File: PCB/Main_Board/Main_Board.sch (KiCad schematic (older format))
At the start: 12 parts, among them J1 USB_B_Micro, J2 Screw_Terminal_01x02, J3 SJ1-3523N, J4 SJ1-3523N, J5 Screw_Terminal_01x04, J6 Screw_Terminal_01x06, SW1 SW_SPDT, U1 TLV75533PDBV

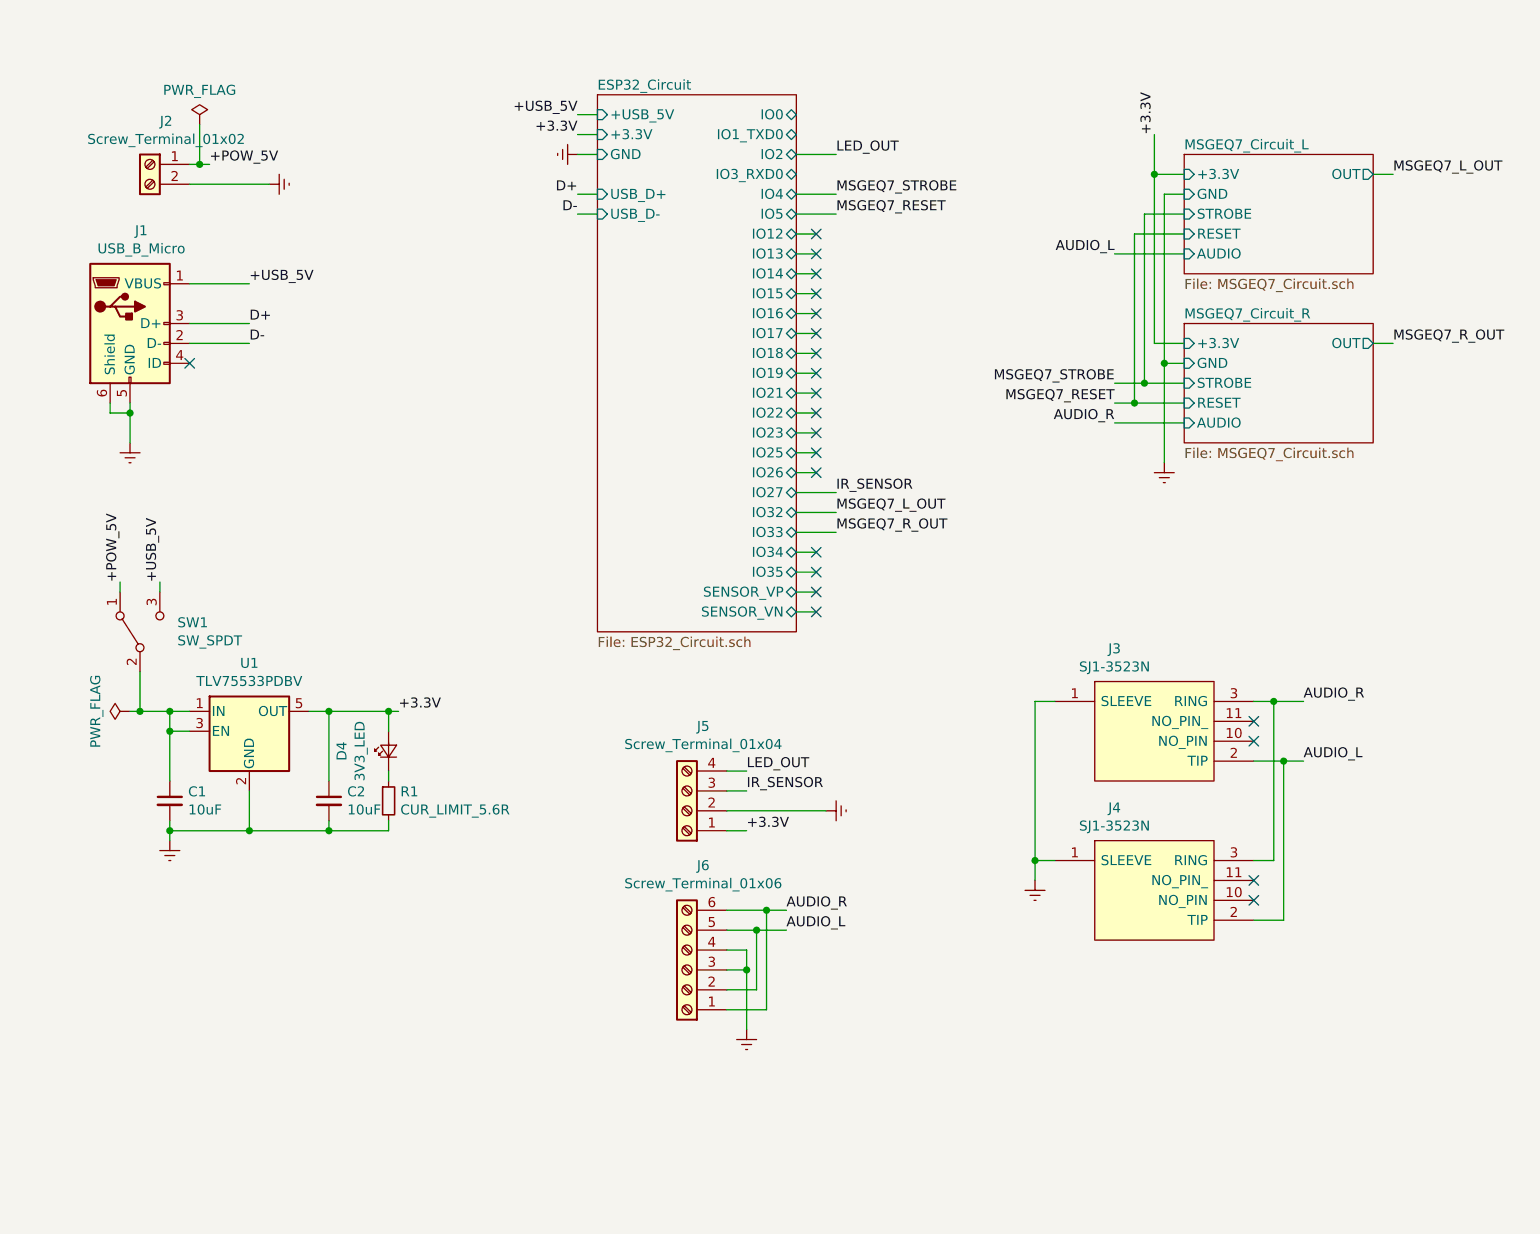
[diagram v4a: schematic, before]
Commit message: Add level shifter and further PCB work
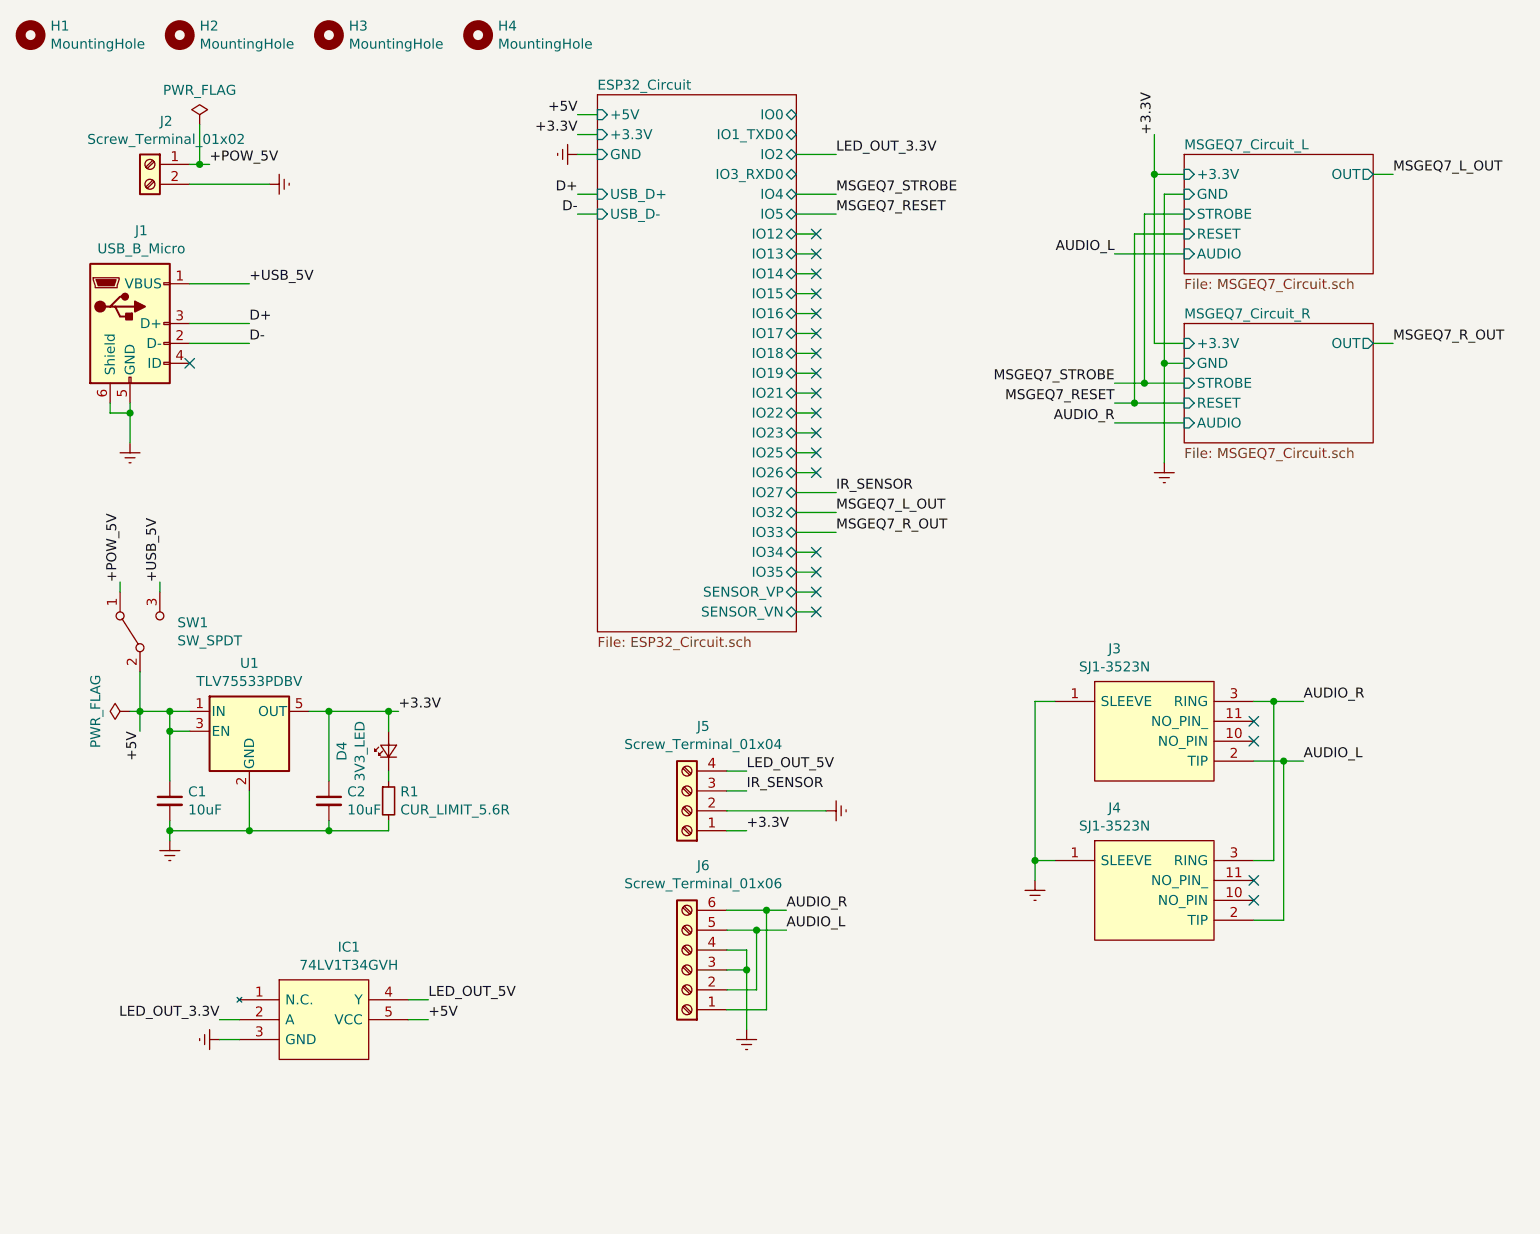
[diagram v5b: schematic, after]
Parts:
- added H1, H2, H3, H4: MountingHole, MountingHole:MountingHole_3.2mm_M3, symbol Mechanical:MountingHole
- added IC1: 74LV1T34GVH, SamacSys:SOT95P275X110-5N, symbol SamacSys:74LV1T34GVH
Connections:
- net Earth: now also IC1.3 (GND)
- net +5V: now reaches C1.1, SW1.2 (B), U1.1 (IN), U1.3 (EN)
- net +5V: now also IC1.5 (VCC)
- net LED_OUT renamed LED_OUT_5V
- net LED_OUT_5V: now also IC1.4 (Y)
- new net LED_OUT_3.3V: IC1.2 (A)
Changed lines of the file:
@@
 F1 "ESP32_Circuit.sch" 50
 F2 "+3.3V" I L 3500 1150 50
-F3 "+USB_5V" I L 3500 1050 50
-F4 "GND" I L 3500 1250 50
-F5 "USB_D-" I L 3500 1550 50
-F6 "USB_D+" I L 3500 1450 50
-F7 "IO35" B R 4500 3350 50
-F8 "IO33" B R 4500 3150 50
-F9 "IO34" B R 4500 3250 50
-F10 "IO32" B R 4500 3050 50
-F11 "IO27" B R 4500 2950 50
-F12 "IO26" B R 4500 2850 50
-F13 "IO25" B R 4500 2750 50
-F14 "IO23" B R 4500 2650 50
-F15 "IO22" B R 4500 2550 50
-F16 "IO21" B R 4500 2450 50
-F17 "IO19" B R 4500 2350 50
-F18 "IO18" B R 4500 2250 50
-F19 "IO17" B R 4500 2150 50
-F20 "IO16" B R 4500 2050 50
-F21 "IO15" B R 4500 1950 50
-F22 "IO14" B R 4500 1850 50
-F23 "IO13" B R 4500 1750 50
-F24 "IO12" B R 4500 1650 50
-F25 "IO5" B R 4500 1550 50
-F26 "IO4" B R 4500 1450 50
-F27 "IO2" B R 4500 1250 50
-F28 "IO3_RXD0" B R 4500 1350 50
-F29 "IO1_TXD0" B R 4500 1150 50
-F30 "IO0" B R 4500 1050 50
-F31 "SENSOR_VP" B R 4500 3450 50
-F32 "SENSOR_VN" B R 4500 3550 50
+F3 "GND" I L 3500 1250 50
+F4 "USB_D-" I L 3500 1550 50
+F5 "USB_D+" I L 3500 1450 50
+F6 "IO35" B R 4500 3350 50
+F7 "IO33" B R 4500 3150 50
+F8 "IO34" B R 4500 3250 50
+F9 "IO32" B R 4500 3050 50
+F10 "IO27" B R 4500 2950 50
+F11 "IO26" B R 4500 2850 50
+F12 "IO25" B R 4500 2750 50
+F13 "IO23" B R 4500 2650 50
+F14 "IO22" B R 4500 2550 50
+F15 "IO21" B R 4500 2450 50
+F16 "IO19" B R 4500 2350 50
+F17 "IO18" B R 4500 2250 50
+F18 "IO17" B R 4500 2150 50
+F19 "IO16" B R 4500 2050 50
+F20 "IO15" B R 4500 1950 50
+F21 "IO14" B R 4500 1850 50
+F22 "IO13" B R 4500 1750 50
+F23 "IO12" B R 4500 1650 50
+F24 "IO5" B R 4500 1550 50
+F25 "IO4" B R 4500 1450 50
+F26 "IO2" B R 4500 1250 50
+F27 "IO3_RXD0" B R 4500 1350 50
+F28 "IO1_TXD0" B R 4500 1150 50
+F29 "IO0" B R 4500 1050 50
+F30 "SENSOR_VP" B R 4500 3450 50
+F31 "SENSOR_VN" B R 4500 3550 50
+F32 "+5V" I L 3500 1050 50
 $EndSheet
 Text Label 3400 1050 2    50   ~ 0
-+USB_5V
++5V
 Text Label 3400 1150 2    50   ~ 0
 +3.3V
@@
 MSGEQ7_STROBE
 Text Label 4250 4350 0    50   ~ 0
-LED_OUT
+LED_OUT_5V
 Text Label 4700 3050 0    50   ~ 0
 MSGEQ7_L_OUT
@@
 	4500 3150 4700 3150
 Text Label 4700 1250 0    50   ~ 0
-LED_OUT
+LED_OUT_3.3V
 Wire Wire Line
 	4500 1250 4700 1250
@@
 Wire Wire Line
 	4150 4550 4650 4550
+Text Label 1200 4150 3    50   ~ 0
++5V
+Wire Wire Line
+	1200 4150 1200 4050
+$Comp
+L SamacSys:74LV1T34GVH IC1
+U 1 1 5F6C379F
+P 1700 5500
+F 0 "IC1" H 2250 5765 50  0000 C CNN
+F 1 "74LV1T34GVH" H 2250 5674 50  0000 C CNN
+F 2 "SamacSys:SOT95P275X110-5N" H 2650 5600 50  0001 L CNN
+F 3 "https://assets.nexperia.com/documents/data-sheet/74LV1T34.pdf" H 2650 5500 50  0001 L CNN
+F 4 "Buffers & Line Drivers BUFFER LINE DRIVER" H 2650 5400 50  0001 L CNN "Description"
+F 5 "1.1" H 2650 5300 50  0001 L CNN "Height"
+F 6 "771-74LV1T34GVH" H 2650 5200 50  0001 L CNN "Mouser Part Number"
+F 7 "https://www.mouser.co.uk/ProductDetail/Nexperia/74LV1T34GVH?qs=Cb2nCFKsA8oBEV51cGATww%3D%3D" H 2650 5100 50  0001 L CNN "Mouser Price/Stock"
+F 8 "Nexperia" H 2650 5000 50  0001 L CNN "Manufacturer_Name"
+F 9 "74LV1T34GVH" H 2650 4900 50  0001 L CNN "Manufacturer_Part_Number"
+	1    1700 5500
+	1    0    0    -1
+$EndComp
+Text Label 2650 5600 0    50   ~ 0
++5V
+Wire Wire Line
+	2650 5600 2550 5600
+$Comp
+L power:Earth #PWR0102
+U 1 1 5F6E2BBD
+P 1600 5700
+AR Path="/5F6E2BBD" Ref="#PWR0102"  Part="1"
+AR Path="/5F591C5D/5F6E2BBD" Ref="#PWR?"  Part="1"
+F 0 "#PWR0102" H 1600 5450 50  0001 C CNN
+F 1 "Earth" H 1600 5550 50  0001 C CNN
+F 2 "" H 1600 5700 50  0001 C CNN
+F 3 "~" H 1600 5700 50  0001 C CNN
+	1    1600 5700
+	0    1    1    0
+$EndComp
+Wire Wire Line
+	1600 5700 1700 5700
+Text Label 1600 5600 2    50   ~ 0
+LED_OUT_3.3V
+Wire Wire Line
+	1600 5600 1700 5600
+Text Label 2650 5500 0    50   ~ 0
+LED_OUT_5V
+Wire Wire Line
+	2650 5500 2550 5500
+$Comp
+L Mechanical:MountingHole H1
+U 1 1 5F70586C
+P 650 650
+F 0 "H1" H 750 696 50  0000 L CNN
+F 1 "MountingHole" H 750 605 50  0000 L CNN
+F 2 "MountingHole:MountingHole_3.2mm_M3" H 650 650 50  0001 C CNN
+F 3 "~" H 650 650 50  0001 C CNN
+	1    650  650
+	1    0    0    -1
+$EndComp
+$Comp
+L Mechanical:MountingHole H2
+U 1 1 5F706754
+P 1400 650
+F 0 "H2" H 1500 696 50  0000 L CNN
+F 1 "MountingHole" H 1500 605 50  0000 L CNN
+F 2 "MountingHole:MountingHole_3.2mm_M3" H 1400 650 50  0001 C CNN
+F 3 "~" H 1400 650 50  0001 C CNN
+	1    1400 650
+	1    0    0    -1
+$EndComp
+$Comp
+L Mechanical:MountingHole H3
+U 1 1 5F70733F
+P 2150 650
+F 0 "H3" H 2250 696 50  0000 L CNN
+F 1 "MountingHole" H 2250 605 50  0000 L CNN
+F 2 "MountingHole:MountingHole_3.2mm_M3" H 2150 650 50  0001 C CNN
+F 3 "~" H 2150 650 50  0001 C CNN
+	1    2150 650
+	1    0    0    -1
+$EndComp
+$Comp
+L Mechanical:MountingHole H4
+U 1 1 5F70788E
+P 2900 650
+F 0 "H4" H 3000 696 50  0000 L CNN
+F 1 "MountingHole" H 3000 605 50  0000 L CNN
+F 2 "MountingHole:MountingHole_3.2mm_M3" H 2900 650 50  0001 C CNN
+F 3 "~" H 2900 650 50  0001 C CNN
+	1    2900 650
+	1    0    0    -1
+$EndComp
 $EndSCHEMATC

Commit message: Finish PCB, add missing models, change switch
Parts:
- removed H4: MountingHole, MountingHole:MountingHole_3.2mm_M3, symbol Mechanical:MountingHole
- added U2: Artwork, Artwork:dog_logo, symbol Artwork:Artwork
- J1: footprint Connector_USB:USB_Micro-B_Amphenol_10103594-0001LF_Horizontal -> SamacSys:AMPHENOL_10118194-0001LF
- SW1: footprint SamacSys:CS12ANW03 -> SamacSys:25136NAH
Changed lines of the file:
@@
 encoding utf-8
 Sheet 1 4
-Title ""
-Date ""
-Rev ""
-Comp ""
+Title "LED Matrix Control Board"
+Date "2020-09-08"
+Rev "v1.0"
+Comp "Richard Carter"
 Comment1 ""
 Comment2 ""
@@
 F 0 "J1" H 1207 2567 50  0000 C CNN
 F 1 "USB_B_Micro" H 1207 2476 50  0000 C CNN
-F 2 "Connector_USB:USB_Micro-B_Amphenol_10103594-0001LF_Horizontal" H 1300 2050 50  0001 C CNN
+F 2 "SamacSys:AMPHENOL_10118194-0001LF" H 1300 2050 50  0001 C CNN
 F 3 "~" H 1300 2050 50  0001 C CNN
 F 4 "https://www.mouser.co.uk/ProductDetail/Amphenol-FCI/10118194-0001LF?qs=Ywefl8B65e4FIdY8OWfRQA%3D%3D" H 1150 2100 50  0001 C CNN "Product"
@@
 F 0 "SW1" V 1246 3462 50  0000 R CNN
 F 1 "SW_SPDT" V 1155 3462 50  0000 R CNN
-F 2 "SamacSys:CS12ANW03" H 1200 3650 50  0001 C CNN
+F 2 "SamacSys:25136NAH" H 1200 3650 50  0001 C CNN
 F 3 "~" H 1200 3650 50  0001 C CNN
 F 4 "https://www.mouser.co.uk/ProductDetail/NKK-Switches/CS12ANW03?qs=4P1McwaGddbVHu%252BBZT0egw%3D%3D" V 1200 3650 50  0001 C CNN "Product"
@@
 Wire Wire Line
 	1100 3400 1100 3450
-Wire Wire Line
-	1300 3400 1300 3450
 Text Label 1750 1900 0    50   ~ 0
-+USB_5V
-Text Label 1300 3400 1    50   ~ 0
 +USB_5V
 Text Label 1100 3400 1    50   ~ 0
@@
 $EndComp
 $Comp
-L Mechanical:MountingHole H4
-U 1 1 5F70788E
-P 2900 650
-F 0 "H4" H 3000 696 50  0000 L CNN
-F 1 "MountingHole" H 3000 605 50  0000 L CNN
-F 2 "MountingHole:MountingHole_3.2mm_M3" H 2900 650 50  0001 C CNN
-F 3 "~" H 2900 650 50  0001 C CNN
-	1    2900 650
-	1    0    0    -1
-$EndComp
+L Artwork:Artwork U2
+U 1 1 5F584C25
+P 1050 6350
+F 0 "U2" H 1338 6401 50  0000 L CNN
+F 1 "Artwork" H 1338 6310 50  0000 L CNN
+F 2 "Artwork:dog_logo" H 1050 6700 50  0001 C CNN
+F 3 "" H 1050 6700 50  0001 C CNN
+	1    1050 6350
+	1    0    0    -1
+$EndComp
+Wire Wire Line
+	1300 3400 1300 3450
+Text Label 1300 3400 1    50   ~ 0
++USB_5V
 $EndSCHEMATC

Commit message: Fix plane routing and change dog icon
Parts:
- U2: footprint Artwork:dog_logo -> Artwork:dog_2_small
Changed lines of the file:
@@
 F 0 "U2" H 1338 6401 50  0000 L CNN
 F 1 "Artwork" H 1338 6310 50  0000 L CNN
-F 2 "Artwork:dog_logo" H 1050 6700 50  0001 C CNN
+F 2 "Artwork:dog_2_small" H 1050 6700 50  0001 C CNN
 F 3 "" H 1050 6700 50  0001 C CNN
 	1    1050 6350

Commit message: Add new art and JLC order number under ESP32-WROOM-32
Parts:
- added ART2: Artwork, Artwork:cat_small_mirrored, symbol Artwork:Artwork
- renumbered U2 to ART1
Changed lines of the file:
@@
 $EndComp
 $Comp
-L Artwork:Artwork U2
+L Artwork:Artwork ART1
 U 1 1 5F584C25
 P 1050 6350
-F 0 "U2" H 1338 6401 50  0000 L CNN
+F 0 "ART1" H 1338 6401 50  0000 L CNN
 F 1 "Artwork" H 1338 6310 50  0000 L CNN
 F 2 "Artwork:dog_2_small" H 1050 6700 50  0001 C CNN
@@
 Text Label 1300 3400 1    50   ~ 0
 +USB_5V
+$Comp
+L Artwork:Artwork ART2
+U 1 1 5F59357E
+P 2000 6350
+F 0 "ART2" H 2288 6401 50  0000 L CNN
+F 1 "Artwork" H 2288 6310 50  0000 L CNN
+F 2 "Artwork:cat_small_mirrored" H 2000 6700 50  0001 C CNN
+F 3 "" H 2000 6700 50  0001 C CNN
+	1    2000 6350
+	1    0    0    -1
+$EndComp
 $EndSCHEMATC
